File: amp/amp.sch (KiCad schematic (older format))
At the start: 48 parts, among them J1 Conn_01x03, J2 DUAL_RCA, SW1 SW_SPST, T1 Transformer_1P_1S, T2 Transformer_1P_1S, T3 Transformer_PT190.2, U1 6CY7, U2 6CY7, U3 6CA4

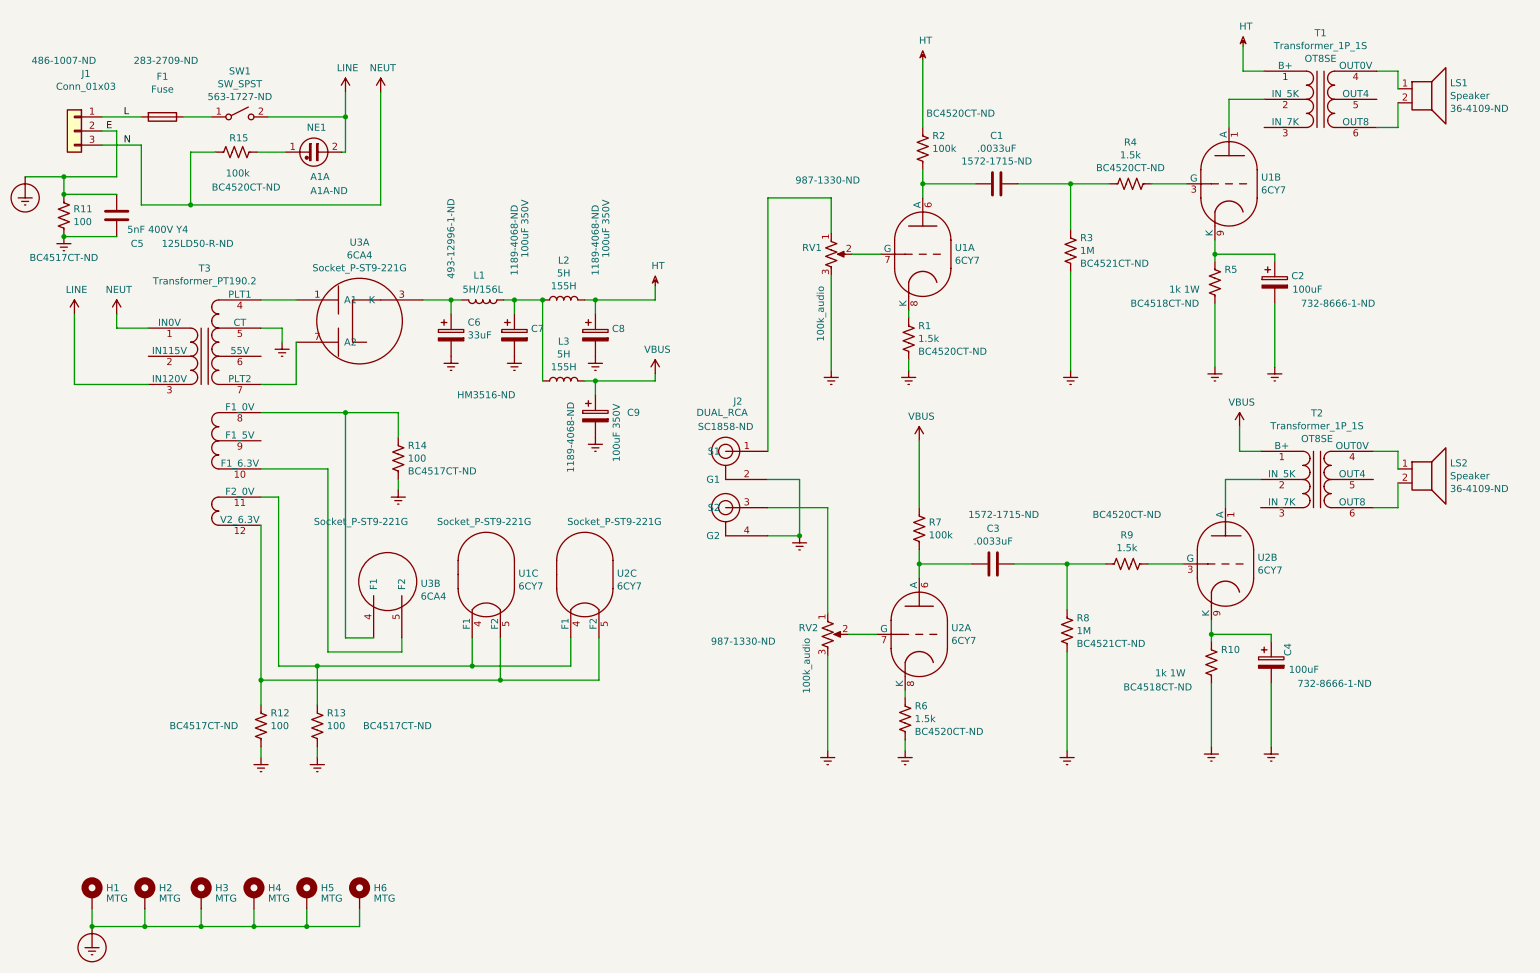
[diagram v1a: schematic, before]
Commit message: First draft layout done
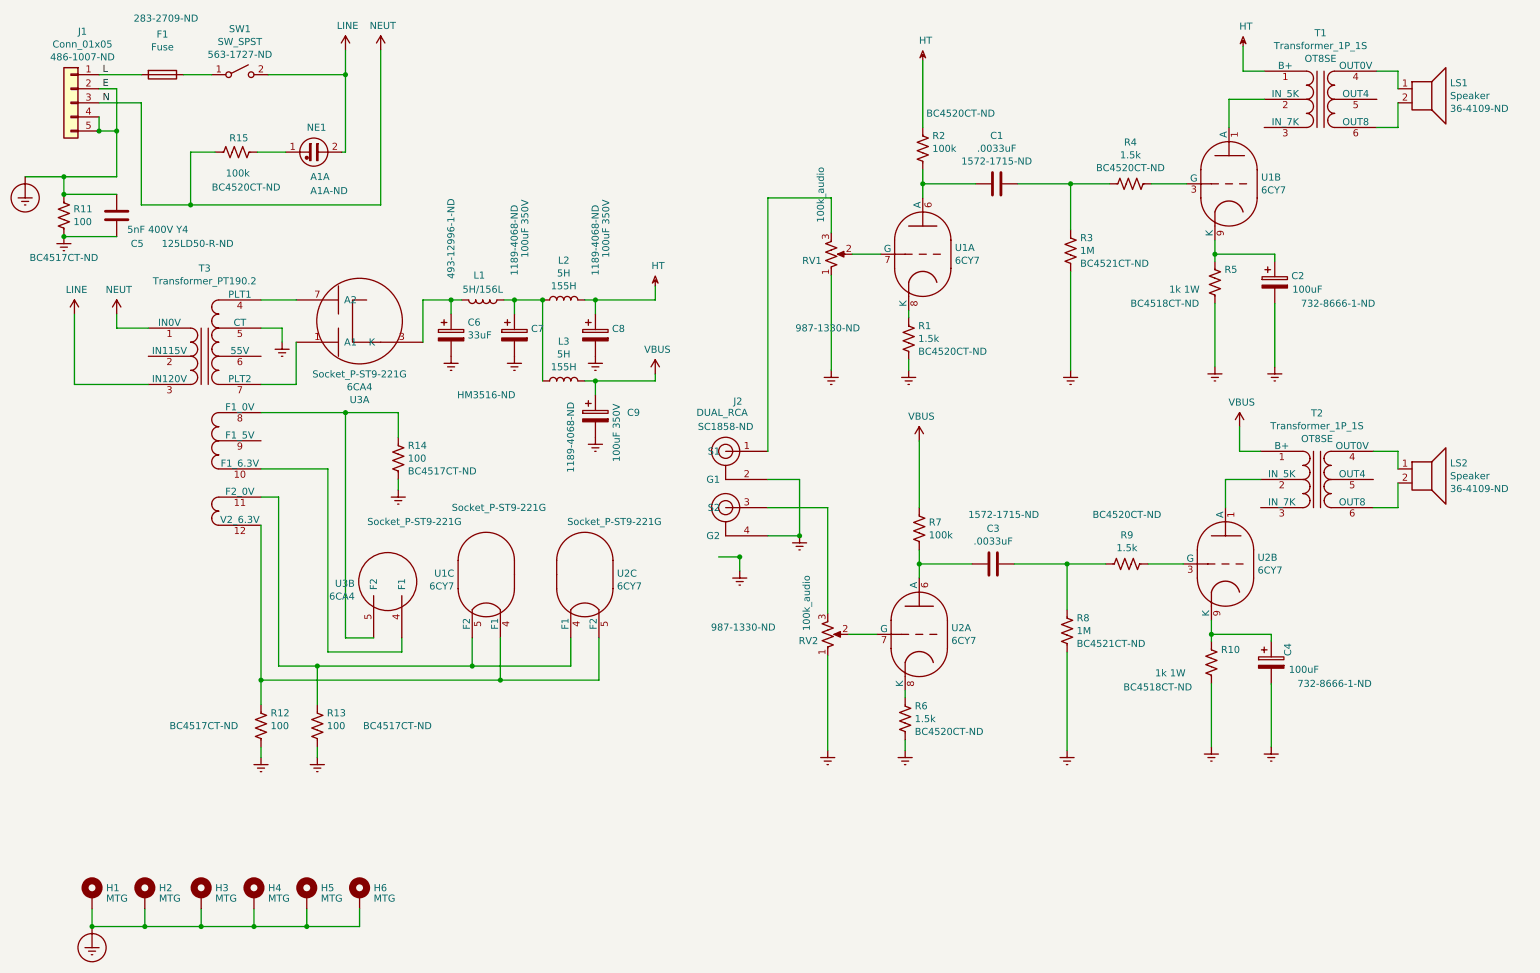
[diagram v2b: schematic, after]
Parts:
- removed J1: Conn_01x03, GSP1_power_entry:GSP1.8101.1, symbol Connector_Generic:Conn_01x03
- added J1: Conn_01x05, GSP1_power_entry:GSP1.8101.1, symbol Connector_Generic:Conn_01x05
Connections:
- net Earth: now also J2.5 (G1), J2.6 (G2), RV1.1, RV2.1; no longer RV1.3, RV2.3
- net Earth_Protective: now also J1.2 (Pin_2), J1.4 (Pin_4), J1.5 (Pin_5)
- net L: now also J1.1 (Pin_1)
- net NEUT: now also J1.3 (Pin_3)
- net at R13.1, T3.11 (F2_0V), U2.4 (F1): now also U1.5 (F2); no longer U1.4 (F1)
- net at R12.1, T3.12 (V2_6.3V), U2.5 (F2): now also U1.4 (F1); no longer U1.5 (F2)
- net at J2.1 (S1): now also RV1.3; no longer RV1.1
- net at J2.3 (S2): now also RV2.3; no longer RV2.1
- net at U3.1 (A1): now also T3.7 (PLT2); no longer T3.4 (PLT1)
- net at U3.7 (A2): now also T3.4 (PLT1); no longer T3.7 (PLT2)
- net at R14.1, T3.8 (F1_0V): now also U3.5 (F2); no longer U3.4 (F1)
- net at T3.10 (F1_6.3V): now also U3.4 (F1); no longer U3.5 (F2)
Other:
- moved on the sheet: F1, SW1
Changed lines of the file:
@@
 F 2 "Valve:Valve_Noval_P" H 4245 4400 50  0001 C CNN
 F 3 "" H 3975 4800 50  0001 C CNN
-F 4 "Socket_P-ST9-221G" H 3625 5175 50  0000 L CNN "CatNo"
+F 4 "Socket_P-ST9-221G" H 3550 5275 50  0000 L CNN "CatNo"
 F 5 "AES" H 3975 4800 50  0001 C CNN "Vendor"
 	3    3975 4800
-	1    0    0    -1
+	-1   0    0    -1
 $EndComp
 $Comp
@@
 F 5 "DigiKey" H 6425 2525 50  0001 C CNN "Vendor"
 	1    6425 2525
-	1    0    0    -1
+	1    0    0    1
 $EndComp
 Wire Wire Line
@@
 F 5 "DigiKey" H 6400 5225 50  0001 C CNN "Vendor"
 	1    6400 5225
-	1    0    0    -1
+	1    0    0    1
 $EndComp
 Wire Wire Line
@@
 L my_tubes:6CA4 U3
 U 1 1 5FFAF289
-P 2525 2850
-F 0 "U3" H 3075 3259 50  0000 C CNN
-F 1 "6CA4" H 3075 3168 50  0000 C CNN
-F 2 "Valve:Valve_Noval_P" H 2625 2850 50  0001 C CNN
-F 3 "" H 2625 2850 50  0001 C CNN
-F 4 "Socket_P-ST9-221G" H 3075 3077 50  0000 C CNN "CatNo"
-F 5 "AES" H 2525 2850 50  0001 C CNN "Vendor"
-	1    2525 2850
-	1    0    0    -1
+P 2525 3150
+F 0 "U3" H 3075 3559 50  0000 C CNN
+F 1 "6CA4" H 3075 3468 50  0000 C CNN
+F 2 "Valve:Valve_Noval_P" H 2625 3150 50  0001 C CNN
+F 3 "" H 2625 3150 50  0001 C CNN
+F 4 "Socket_P-ST9-221G" H 3075 3377 50  0000 C CNN "CatNo"
+F 5 "AES" H 2525 3150 50  0001 C CNN "Vendor"
+	1    2525 3150
+	1    0    0    1
 $EndComp
 $Comp
 L my_tubes:6CA4 U3
 U 2 1 5FFB06E3
-P 2775 5050
-F 0 "U3" H 3509 5236 50  0000 L CNN
-F 1 "6CA4" H 3509 5145 50  0000 L CNN
-F 2 "Valve:Valve_Noval_P" H 2875 5050 50  0001 C CNN
-F 3 "" H 2875 5050 50  0001 C CNN
-F 4 "Socket_P-ST9-221G" H 2750 5675 50  0000 L CNN "CatNo"
-	2    2775 5050
-	1    0    0    -1
+P 3775 5050
+F 0 "U3" H 4509 5236 50  0000 L CNN
+F 1 "6CA4" H 4509 5145 50  0000 L CNN
+F 2 "Valve:Valve_Noval_P" H 3875 5050 50  0001 C CNN
+F 3 "" H 3875 5050 50  0001 C CNN
+F 4 "Socket_P-ST9-221G" H 3750 5675 50  0000 L CNN "CatNo"
+	2    3775 5050
+	-1   0    0    -1
 $EndComp
 $Comp
@@
 L Device:Fuse F1
 U 1 1 6004FF8D
-P 1675 1550
-F 0 "F1" V 1388 1550 50  0000 C CNN
-F 1 "Fuse" V 1479 1550 50  0000 C CNN
-F 2 "HBH_fuse_holder:HBH-I-R" V 1605 1550 50  0001 C CNN
-F 3 "~" H 1675 1550 50  0001 C CNN
-F 4 "283-2709-ND" V 1275 1575 50  0000 C CNN "CatNo"
-F 5 "DigiKey" V 1675 1550 50  0001 C CNN "Vendor"
-	1    1675 1550
+P 1675 1250
+F 0 "F1" V 1388 1250 50  0000 C CNN
+F 1 "Fuse" V 1479 1250 50  0000 C CNN
+F 2 "HBH_fuse_holder:HBH-I-R" V 1605 1250 50  0001 C CNN
+F 3 "~" H 1675 1250 50  0001 C CNN
+F 4 "283-2709-ND" V 1275 1275 50  0000 C CNN "CatNo"
+F 5 "DigiKey" V 1675 1250 50  0001 C CNN "Vendor"
+	1    1675 1250
 	0    1    1    0
-$EndComp
-$Comp
-L Connector_Generic:Conn_01x03 J1
-U 1 1 60054840
-P 1050 1650
-F 0 "J1" H 968 2057 50  0000 C CNN
-F 1 "Conn_01x03" H 968 1966 50  0000 C CNN
-F 2 "GSP1_power_entry:GSP1.8101.1" H 1050 1650 50  0001 C CNN
-F 3 "~" H 1050 1650 50  0001 C CNN
-F 4 "486-1007-ND" H 1125 2150 50  0000 C CNN "CatNo"
-F 5 "DigiKey" H 1050 1650 50  0001 C CNN "Vendor"
-	1    1050 1650
-	-1   0    0    -1
 $EndComp
 $Comp
 L Switch:SW_SPST SW1
 U 1 1 60059C04
-P 2225 1550
-F 0 "SW1" H 2225 1875 50  0000 C CNN
-F 1 "SW_SPST" H 2225 1784 50  0000 C CNN
-F 2 "Switch_8GA:8GA1016-Z" H 2225 1550 50  0001 C CNN
-F 3 "~" H 2225 1550 50  0001 C CNN
-F 4 "563-1727-ND" H 2225 1693 50  0000 C CNN "CatNo"
-F 5 "DigiKey" H 2225 1550 50  0001 C CNN "Vendor"
-	1    2225 1550
-	1    0    0    -1
-$EndComp
-Wire Wire Line
-	2425 1550 2975 1550
-Wire Wire Line
-	1525 2175 1525 1750
-Wire Wire Line
-	1525 1750 1250 1750
-Wire Wire Line
-	1250 1550 1525 1550
-Wire Wire Line
-	1250 1650 1350 1650
-Wire Wire Line
-	1350 1650 1350 1975
+P 2225 1250
+F 0 "SW1" H 2225 1575 50  0000 C CNN
+F 1 "SW_SPST" H 2225 1484 50  0000 C CNN
+F 2 "Switch_8GA:8GA1016-Z" H 2225 1250 50  0001 C CNN
+F 3 "~" H 2225 1250 50  0001 C CNN
+F 4 "563-1727-ND" H 2225 1393 50  0000 C CNN "CatNo"
+F 5 "DigiKey" H 2225 1250 50  0001 C CNN "Vendor"
+	1    2225 1250
+	1    0    0    -1
+$EndComp
+Wire Wire Line
+	2425 1250 2975 1250
+Wire Wire Line
+	1525 2175 1525 1450
+Wire Wire Line
+	1525 1450 1225 1450
+Wire Wire Line
+	1225 1250 1525 1250
+Wire Wire Line
+	1225 1350 1350 1350
 $Comp
 L power:LINE #PWR018
 U 1 1 6006C7EF
-P 2975 1375
-F 0 "#PWR018" H 2975 1225 50  0001 C CNN
-F 1 "LINE" H 2990 1548 50  0000 C CNN
-F 2 "" H 2975 1375 50  0001 C CNN
-F 3 "" H 2975 1375 50  0001 C CNN
-	1    2975 1375
-	1    0    0    -1
-$EndComp
-Wire Wire Line
-	2975 1375 2975 1550
+P 2975 1075
+F 0 "#PWR018" H 2975 925 50  0001 C CNN
+F 1 "LINE" H 2990 1248 50  0000 C CNN
+F 2 "" H 2975 1075 50  0001 C CNN
+F 3 "" H 2975 1075 50  0001 C CNN
+	1    2975 1075
+	1    0    0    -1
+$EndComp
+Wire Wire Line
+	2975 1075 2975 1250
 $Comp
 L power:NEUT #PWR020
 U 1 1 600765B4
-P 3225 1375
-F 0 "#PWR020" H 3225 1225 50  0001 C CNN
-F 1 "NEUT" H 3240 1548 50  0000 C CNN
-F 2 "" H 3225 1375 50  0001 C CNN
-F 3 "" H 3225 1375 50  0001 C CNN
-	1    3225 1375
-	1    0    0    -1
-$EndComp
-Wire Wire Line
-	3225 1375 3225 2175
+P 3225 1075
+F 0 "#PWR020" H 3225 925 50  0001 C CNN
+F 1 "NEUT" H 3240 1248 50  0000 C CNN
+F 2 "" H 3225 1075 50  0001 C CNN
+F 3 "" H 3225 1075 50  0001 C CNN
+	1    3225 1075
+	1    0    0    -1
+$EndComp
+Wire Wire Line
+	3225 1075 3225 2175
 Wire Wire Line
 	1575 3050 1350 3050
@@
 $EndComp
 Connection ~ 975  2400
-Text Label 1400 1550 0    50   ~ 0
+Text Label 1250 1250 0    50   ~ 0
 L
-Text Label 1400 1750 0    50   ~ 0
+Text Label 1250 1450 0    50   ~ 0
 N
-Text Label 1275 1650 0    50   ~ 0
+Text Label 1250 1350 0    50   ~ 0
 E
 Wire Wire Line
-	1825 1550 2025 1550
+	1825 1250 2025 1250
 $Comp
 L my_tubes:DUAL_RCA J2
@@
 Wire Wire Line
 	2850 4050 2375 4050
-Wire Wire Line
-	2375 5550 2375 4450
 Connection ~ 2375 5550
 Wire Wire Line
@@
 	1525 2175 1875 2175
 Wire Wire Line
-	2975 1550 2975 1800
+	2975 1250 2975 1800
 Wire Wire Line
 	2975 1800 2950 1800
-Connection ~ 2975 1550
+Connection ~ 2975 1250
 Wire Wire Line
 	2350 1800 2550 1800
@@
 $EndComp
 Connection ~ 1175 7300
+Wire Wire Line
+	3525 3150 3525 2850
+$Comp
+L Connector_Generic:Conn_01x05 J1
+U 1 1 5FFCDA0D
+P 1025 1450
+F 0 "J1" H 943 1957 50  0000 C CNN
+F 1 "Conn_01x05" H 943 1866 50  0000 C CNN
+F 2 "GSP1_power_entry:GSP1.8101.1" H 1025 1450 50  0001 C CNN
+F 3 "~" H 1025 1450 50  0001 C CNN
+F 4 "486-1007-ND" H 943 1775 50  0000 C CNN "CatNo"
+F 5 "DigiKey" H 1025 1450 50  0001 C CNN "Vendor"
+	1    1025 1450
+	-1   0    0    -1
+$EndComp
+Wire Wire Line
+	2375 4450 2375 5550
+Wire Wire Line
+	1225 1550 1225 1650
+Wire Wire Line
+	1225 1650 1350 1650
+Wire Wire Line
+	1350 1350 1350 1650
+Connection ~ 1225 1650
+Connection ~ 1350 1650
+Wire Wire Line
+	1350 1650 1350 1975
+Wire Wire Line
+	5625 4675 5775 4675
+Wire Wire Line
+	5775 4675 5775 4775
+Connection ~ 5775 4675
+$Comp
+L power:Earth #PWR0103
+U 1 1 6005E88B
+P 5775 4775
+F 0 "#PWR0103" H 5775 4525 50  0001 C CNN
+F 1 "Earth" H 5775 4625 50  0001 C CNN
+F 2 "" H 5775 4775 50  0001 C CNN
+F 3 "~" H 5775 4775 50  0001 C CNN
+	1    5775 4775
+	1    0    0    -1
+$EndComp
 $EndSCHEMATC

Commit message: Candidate for first build
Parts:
- removed SW1: SW_SPST, Switch_8GA:8GA1016-Z, symbol Switch:SW_SPST
- added SW1: SW_SPST_GND, Switch_8GA:8GA1016-Z, symbol my_tubes:SW_SPST_GND
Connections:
- net Earth_Protective: now also SW1.4 (G1), SW1.5 (G2)
- net LINE: now also SW1.2 (B)
- net at F1.1: now also SW1.1 (A)
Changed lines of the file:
@@
 	0    1    1    0
-$EndComp
-$Comp
-L Switch:SW_SPST SW1
-U 1 1 60059C04
-P 2225 1250
-F 0 "SW1" H 2225 1575 50  0000 C CNN
-F 1 "SW_SPST" H 2225 1484 50  0000 C CNN
-F 2 "Switch_8GA:8GA1016-Z" H 2225 1250 50  0001 C CNN
-F 3 "~" H 2225 1250 50  0001 C CNN
-F 4 "563-1727-ND" H 2225 1393 50  0000 C CNN "CatNo"
-F 5 "DigiKey" H 2225 1250 50  0001 C CNN "Vendor"
-	1    2225 1250
-	1    0    0    -1
 $EndComp
 Wire Wire Line
@@
 	1    0    0    -1
 $EndComp
+$Comp
+L my_tubes:SW_SPST_GND SW1
+U 1 1 5FF1D4C9
+P 2225 1250
+F 0 "SW1" H 2225 1575 50  0000 C CNN
+F 1 "SW_SPST_GND" H 2225 1484 50  0000 C CNN
+F 2 "Switch_8GA:8GA1016-Z" H 2225 1250 50  0001 C CNN
+F 3 "~" H 2225 1250 50  0001 C CNN
+F 4 "563-1727-ND" H 2225 1393 50  0000 C CNN "CatNo"
+F 5 "DigiKey" H 2225 1250 50  0001 C CNN "Vendor"
+	1    2225 1250
+	1    0    0    -1
+$EndComp
+Wire Wire Line
+	2275 1400 2175 1400
+Connection ~ 2175 1400
+$Comp
+L power:Earth_Protective #PWR0104
+U 1 1 5FF2E5EE
+P 1950 1400
+F 0 "#PWR0104" H 2200 1150 50  0001 C CNN
+F 1 "Earth_Protective" H 2400 1250 50  0001 C CNN
+F 2 "" H 1950 1300 50  0001 C CNN
+F 3 "~" H 1950 1300 50  0001 C CNN
+	1    1950 1400
+	1    0    0    -1
+$EndComp
+Wire Wire Line
+	1950 1400 2175 1400
 $EndSCHEMATC
